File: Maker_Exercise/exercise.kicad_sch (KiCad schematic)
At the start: 5 parts, among them J1 USB_C_Receptacle_USB2.0_16P, U1 USBLC6-2SC6, U2 STM32G431CBUx

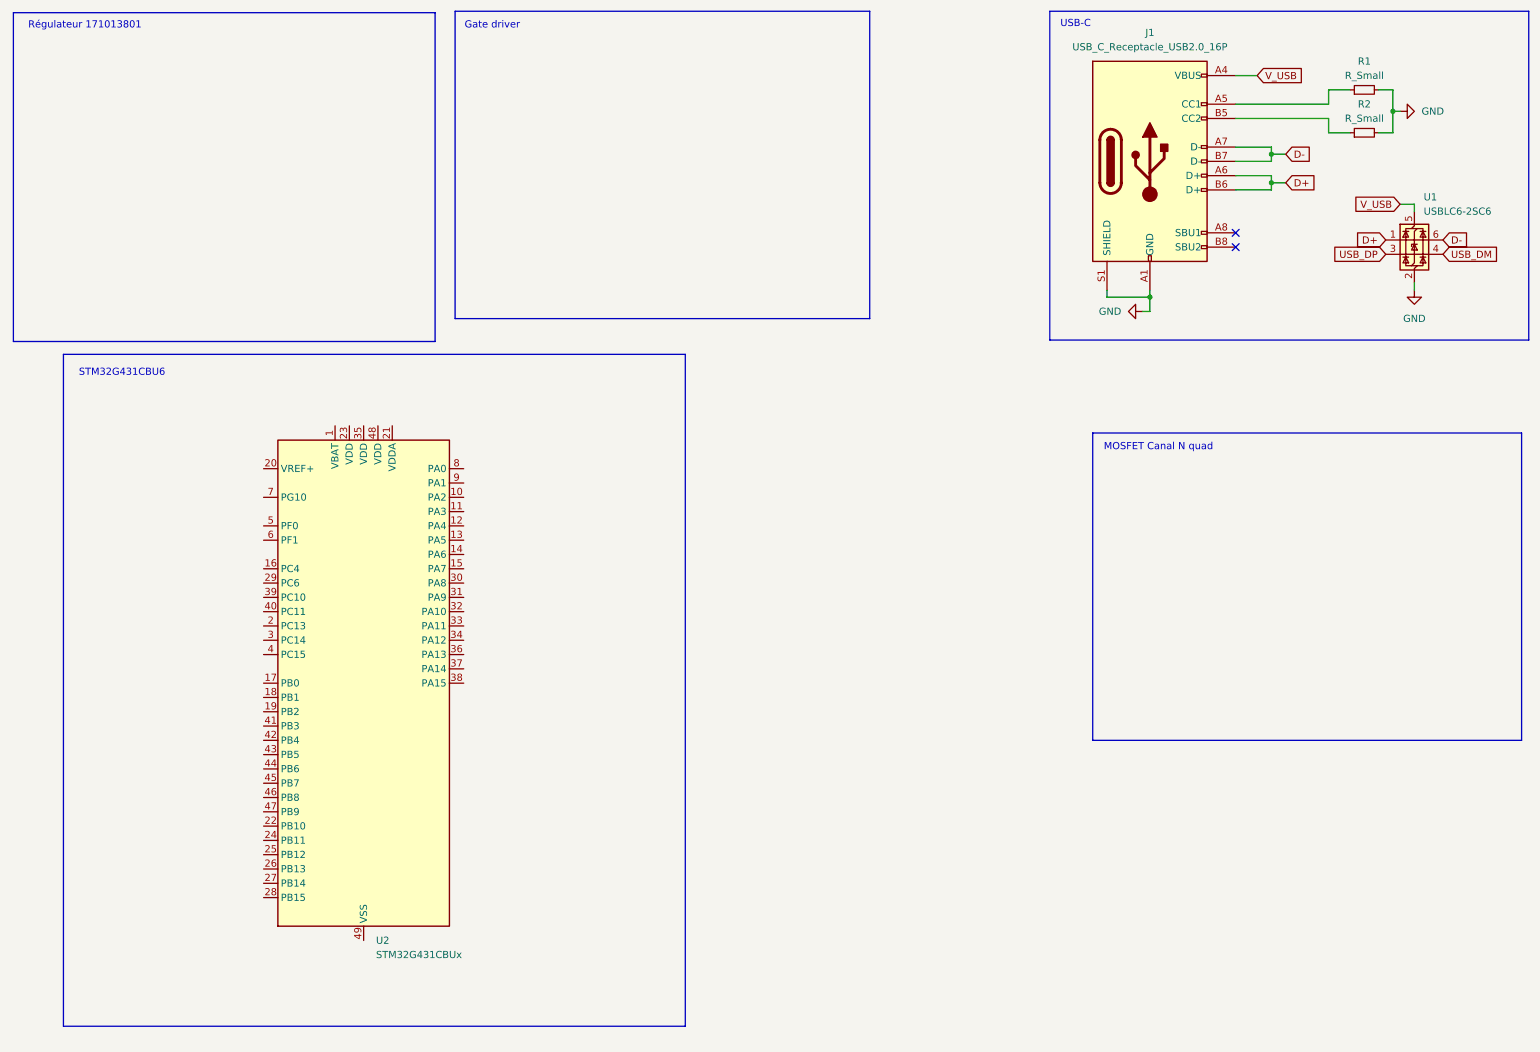
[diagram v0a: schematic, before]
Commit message: Schematic for wurtz voltage regulator
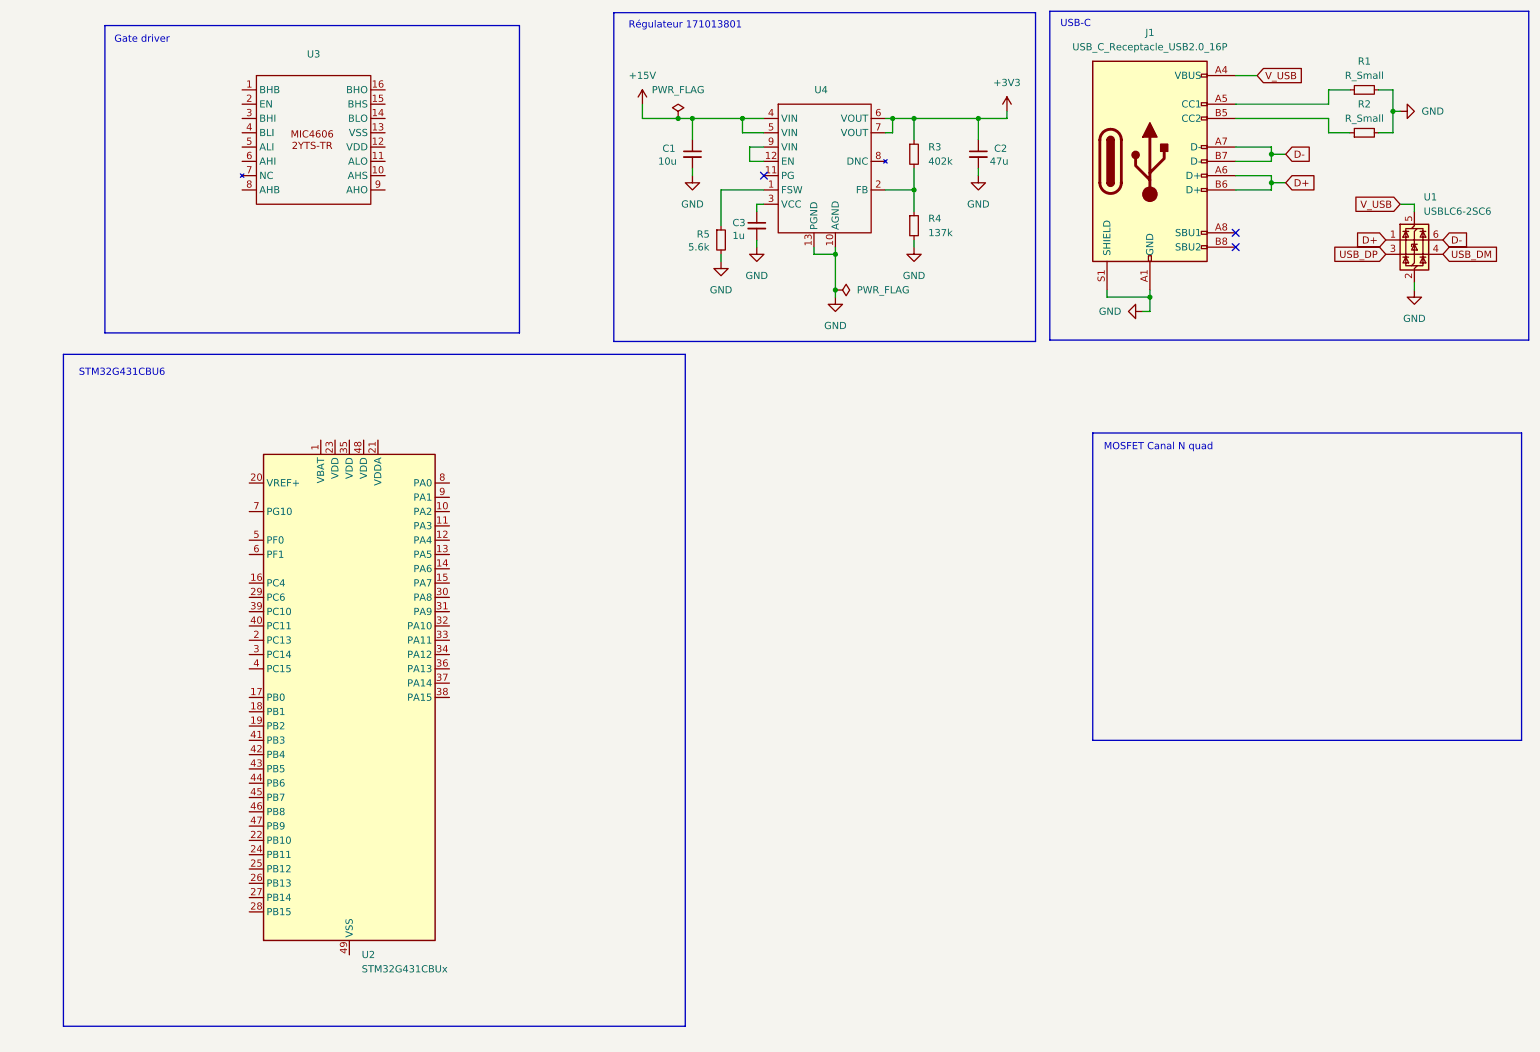
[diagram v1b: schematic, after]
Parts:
- added C1: 10u, symbol Device:C_Small
- added C2: 47u, symbol Device:C_Small
- added C3: 1u, symbol Device:C_Small
- added R3: 402k, symbol Device:R_Small
- added R4: 137k, symbol Device:R_Small
- added R5: 5.6k, symbol Device:R_Small
- added U3: ~, symbol maker:MIC4606-2YTS-TR
- added U4: ~, symbol maker:Regulator_171013801
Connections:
- net GND: now also C1.2, C2.2, C3.2, R4.2, R5.2, U4.10 (AGND), U4.13 (PGND)
- new net: R5.1, U4.1 (FSW)
- new net: U4.12 (EN), U4.9 (VIN)
- new net: R3.2, R4.1, U4.2 (FB)
- new net: C3.1, U4.3 (VCC)
- new net +15V: C1.1, U4.4 (VIN), U4.5 (VIN)
- new net +3V3: C2.1, R3.1, U4.6 (VOUT), U4.7 (VOUT)
- no-connect marks 2 -> 3
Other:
- moved on the sheet: U2

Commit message: Updated schematic
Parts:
- added C10, C14, C8, C9: 100n, symbol Device:C_Small
- added C11: 4u7, symbol Device:C_Small
- added C12, C4, C5, C7: 1u, symbol Device:C_Small
- added C13: 10n, symbol Device:C_Small
- added C6: 2u2, symbol Device:C_Small
- added D1, D2: D_Schottky_Small, symbol Device:D_Schottky_Small
- added J2: Conn_01x02, symbol Connector_Generic:Conn_01x02
- added J3: Conn_ST_STDC14, symbol Connector:Conn_ST_STDC14
- added J4: Conn_01x04, symbol Connector_Generic:Conn_01x04
- added L1: 39n, symbol Device:L_Small
- added U5: ~, symbol maker:FDMQ86530L
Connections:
- net +15V: now also U3.12 (VDD), U3.2 (EN), C6.1, C7.1, J2.1 (Pin_1), J4.3 (Pin_3), U5.11 (D1/D4), U5.2 (D1/D4)
- net +3V3: now also U2.1 (VBAT), U2.23 (VDD), U2.35 (VDD), U2.48 (VDD), C10.1, C11.1, C8.1, C9.1, J3.3 (VCC), L1.1
- net GND: now also U2.20 (VREF+), U2.49 (VSS), U3.13 (VSS), C10.2, C11.2, C12.2, C13.2, C14.2, C6.2, C7.2, C8.2, C9.2, D1.2 (A), D2.2 (A), J2.2 (Pin_2), J3.11 (GNDDetect), J3.5 (GND), J3.7 (GND), J4.4 (Pin_4), U5.5 (S2), U5.6 (S2), U5.7 (S3), U5.8 (S3)
- net +3.3VA: now reaches U2.21 (VDDA)
- net +3.3VA: now also C12.1, C13.1, L1.2
- net UART_DEBUG_TX: now reaches U2.31 (PA9)
- net UART_DEBUG_TX: now also J3.14 (VCP_TX)
- net UART_DEBUG_RX: now reaches U2.32 (PA10)
- net UART_DEBUG_RX: now also J3.13 (VCP_RX)
- net SWDIO: now reaches U2.36 (PA13)
- net SWDIO: now also J3.4 (JTMS/SWDIO)
- net SWCLK: now reaches U2.37 (PA14)
- net SWCLK: now also J3.6 (JCLK/SWCLK)
- net NRST: now reaches U2.7 (PG10)
- net NRST: now also C14.1, J3.12 (~{RST})
- net TIM2_CH1_PWM: now reaches U2.8 (PA0)
- net TIM2_CH1_PWM: now also U3.6 (APWM)
- net TIM2_CH2_PWM: now reaches U2.9 (PA1)
- net TIM2_CH2_PWM: now also U3.3 (BPWM)
- net at U3.1 (BHB): now also C5.2
- net D3/S4_Drive: now reaches U3.10 (AHS)
- net D3/S4_Drive: now also C4.2, D2.1 (K), J4.2 (Pin_2), U5.10 (D3/S4)
- net G3_Drive: now reaches U3.11 (ALO)
- net G3_Drive: now also U5.9 (G3)
- net G2_Drive: now reaches U3.14 (BLO)
- net G2_Drive: now also U5.4 (G2)
- net S1/D2_Drive: now reaches U3.15 (BHS)
- net S1/D2_Drive: now also C5.1, D1.1 (K), J4.1 (Pin_1), U5.3 (S1/D2)
- net G1_Drive: now reaches U3.16 (BHO)
- net G1_Drive: now also U5.1 (G1)
- net at U3.8 (AHB): now also C4.1
- net G4_Drive: now reaches U3.9 (AHO)
- net G4_Drive: now also U5.12 (G4)
- no-connect marks 3 -> 41
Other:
- note added: "Connecteurs"
- company: (none) -> ENSEA
- title: (none) -> Maker_Exercise
- moved on the sheet: C1, C2, C3, R3, R4, R5, U2, U4

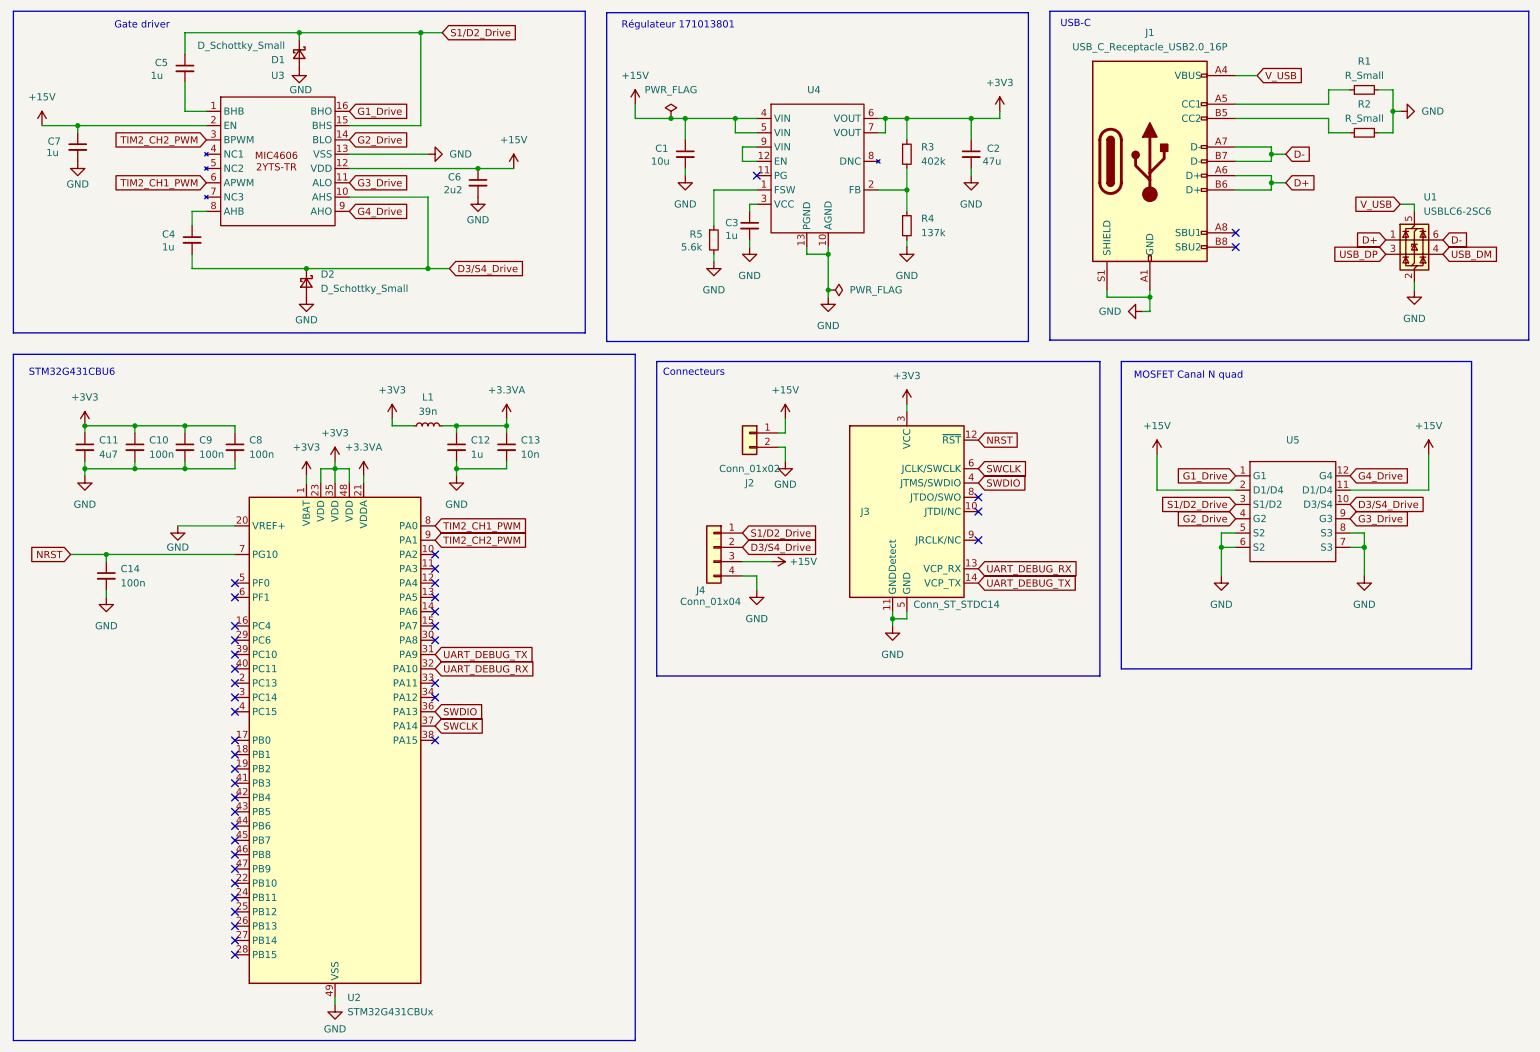
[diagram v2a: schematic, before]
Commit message: finalized schematic and added custom footprints
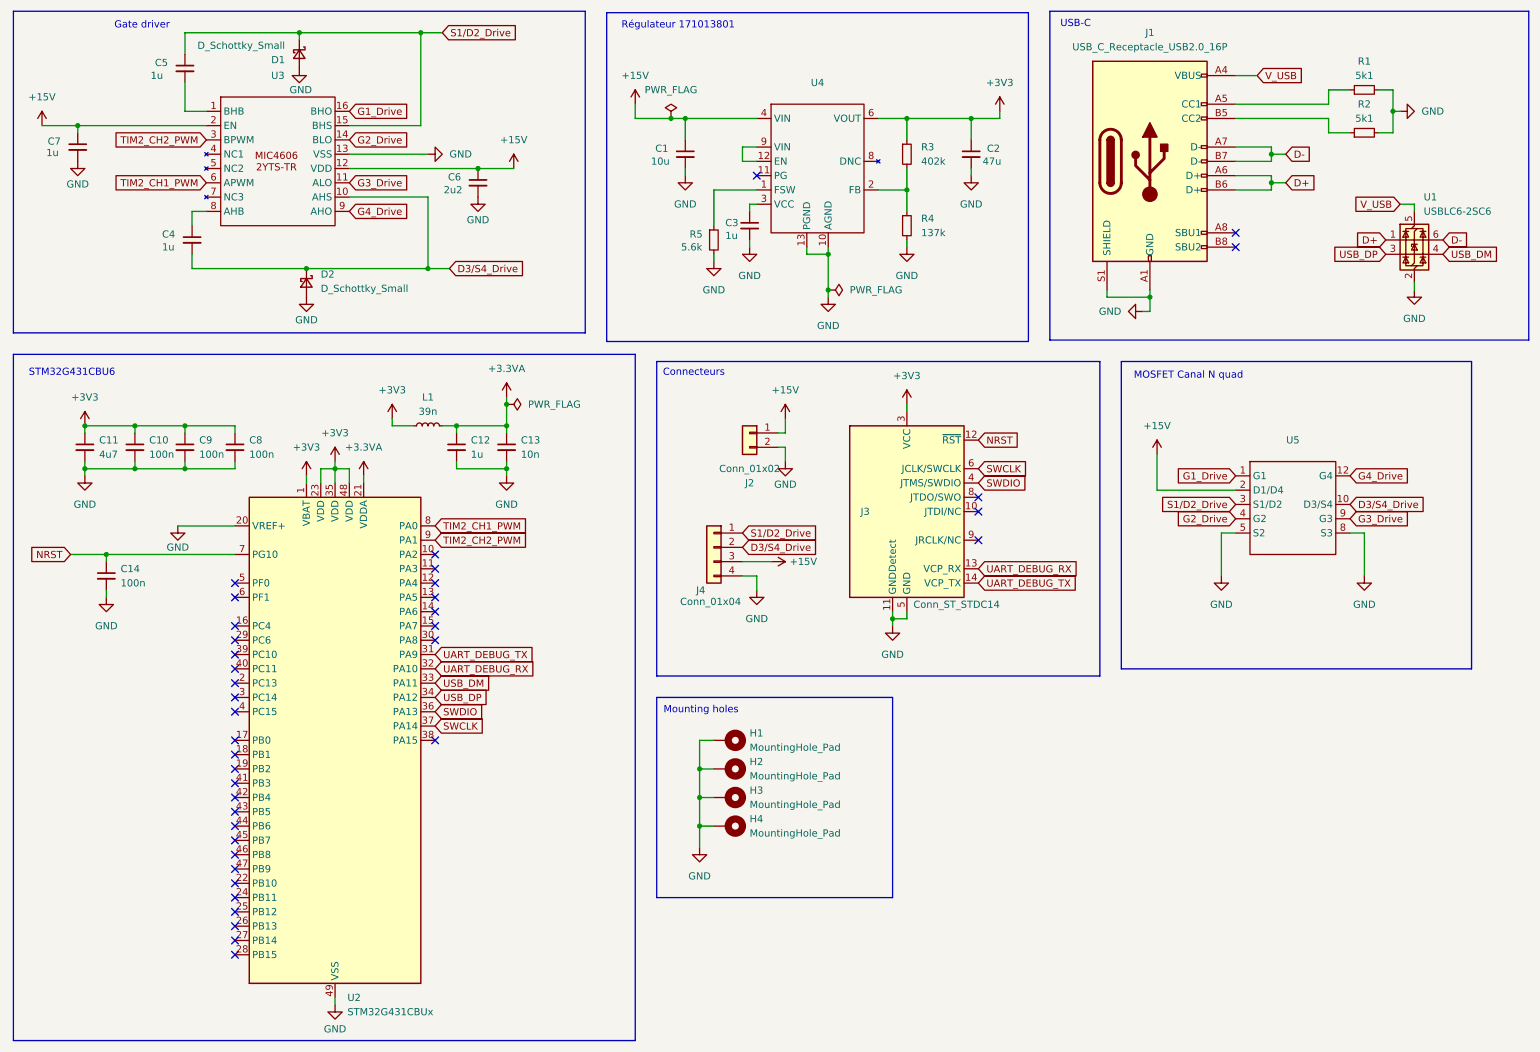
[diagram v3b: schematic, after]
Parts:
- added H1, H2, H3, H4: MountingHole_Pad, MountingHole:MountingHole_3.2mm_M3_DIN965_Pad, symbol Mechanical:MountingHole_Pad
- C1, C10, C11, C12, C13, C14, C2, C3, C4, C5, C6, C7, C8, C9: footprint (none) -> Capacitor_SMD:C_0603_1608Metric_Pad1.08x0.95mm_HandSolder
- D1, D2: footprint (none) -> Diode_SMD:D_0603_1608Metric_Pad1.05x0.95mm_HandSolder
- J1: footprint (none) -> Connector_USB:USB_C_Receptacle_G-Switch_GT-USB-7010ASV
- J2: footprint (none) -> Connector_AMASS:AMASS_XT60-M_1x02_P7.20mm_Vertical
- J3: footprint (none) -> Connector_PinHeader_1.27mm:PinHeader_2x07_P1.27mm_Vertical_SMD
- J4: footprint (none) -> Connector_JST:JST_EH_B4B-EH-A_1x04_P2.50mm_Vertical
- L1: footprint (none) -> Inductor_SMD:L_0805_2012Metric_Pad1.05x1.20mm_HandSolder
- R1, R2: value R_Small -> 5k1; footprint (none) -> Resistor_SMD:R_0603_1608Metric_Pad0.98x0.95mm_HandSolder
- R3, R4, R5: footprint (none) -> Resistor_SMD:R_0603_1608Metric_Pad0.98x0.95mm_HandSolder
- U3: footprint (none) -> Package_SO:TSSOP-16_4.4x5mm_P0.65mm
- U4: footprint (none) -> maker:Regulator_171013801
- U5: footprint (none) -> maker:FDMQ86530L
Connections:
- net +15V: now also U5.13 (D1/D4)
- net D3/S4_Drive: now also U5.15 (D3/S4)
- net GND: now also H1.1, H2.1, H3.1, H4.1
- net S1/D2_Drive: now also U5.14 (S1/D2)
- net USB_DM: now also U2.33 (PA11)
- net USB_DP: now also U2.34 (PA12)
- no-connect marks 41 -> 39
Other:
- note added: "Mounting holes"

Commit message: finalized PCB and routing
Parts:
- added D3, D4: LED_Small, LED_SMD:LED_0603_1608Metric_Pad1.05x0.95mm_HandSolder, symbol Device:LED_Small
- added R6: 820, Resistor_SMD:R_0402_1005Metric_Pad0.72x0.64mm_HandSolder, symbol Device:R_Small
- added R7: 5k6, Resistor_SMD:R_0402_1005Metric_Pad0.72x0.64mm_HandSolder, symbol Device:R_Small
- C1, C10, C11, C12, C13, C14, C2, C3, C4, C5, C6, C7, C8, C9: footprint Capacitor_SMD:C_0603_1608Metric_Pad1.08x0.95mm_HandSolder -> Capacitor_SMD:C_0402_1005Metric_Pad0.74x0.62mm_HandSolder
- R1, R2, R3, R4, R5: footprint Resistor_SMD:R_0603_1608Metric_Pad0.98x0.95mm_HandSolder -> Resistor_SMD:R_0402_1005Metric_Pad0.72x0.64mm_HandSolder
- U2: MPN (none) -> STM32G431CBU6
- U4: MPN (none) -> 171013801
- U5: MPN (none) -> FDMQ86530L
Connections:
- net +15V: now also R7.1
- net +3V3: now also R6.1
- net D+: now also U1.6 (I/O1); no longer U1.1 (I/O1)
- net D-: now also U1.4 (I/O2); no longer U1.6 (I/O1)
- net GND: now also D3.1 (K), D4.1 (K)
- net USB_DM: now also U1.3 (I/O2); no longer U1.4 (I/O2)
- net USB_DP: now also U1.1 (I/O1); no longer U1.3 (I/O2)
- new net: D3.2 (A), R6.2
- new net: D4.2 (A), R7.2
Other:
- note added: "Power LEDs"
